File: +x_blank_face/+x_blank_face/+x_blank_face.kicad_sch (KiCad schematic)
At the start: 0 parts

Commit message: added schematic to +x and routed ish the schematic
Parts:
- added J1: Conn_01x08_Pin, CNN_GNSS_Footprint:DF13-8P, symbol Connector:Conn_01x08_Pin
- added J2, J3: Conn_01x02_Pin, CNN_GNSS_Footprint:TE_440055-2, symbol Connector:Conn_01x02_Pin
- added R1, R2, R3, R4: 75, CNN_GNSS_Footprint:UB3C-75RF1, symbol Device:R
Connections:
- new net +X Drain: J1.3 (Pin_3), J1.4 (Pin_4), R1.2, R2.2, R3.2, R4.2
- new net -X Serial Out: J1.5 (Pin_5), J1.6 (Pin_6), J2.2 (Pin_2), J3.2 (Pin_2)
- new net 12VPDM: J1.1 (Pin_1), J1.2 (Pin_2), R1.1, R2.1, R3.1, R4.1
- new net GND: J1.7 (Pin_7), J1.8 (Pin_8), J2.1 (Pin_1), J3.1 (Pin_1)

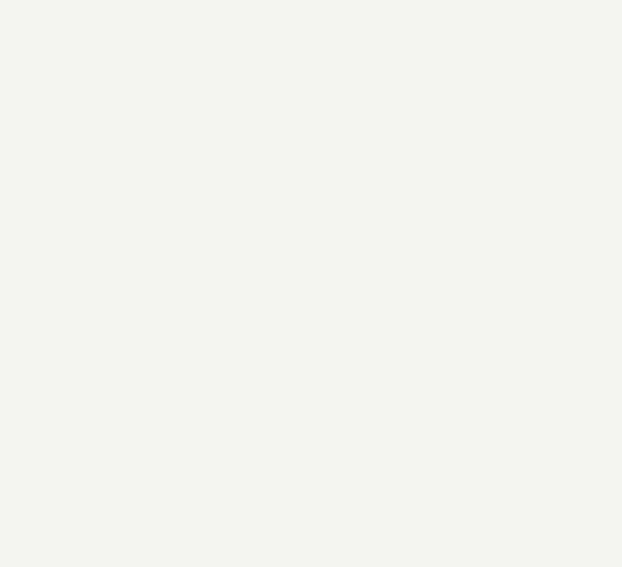
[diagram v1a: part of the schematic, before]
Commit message: Moved some things around, locked some components
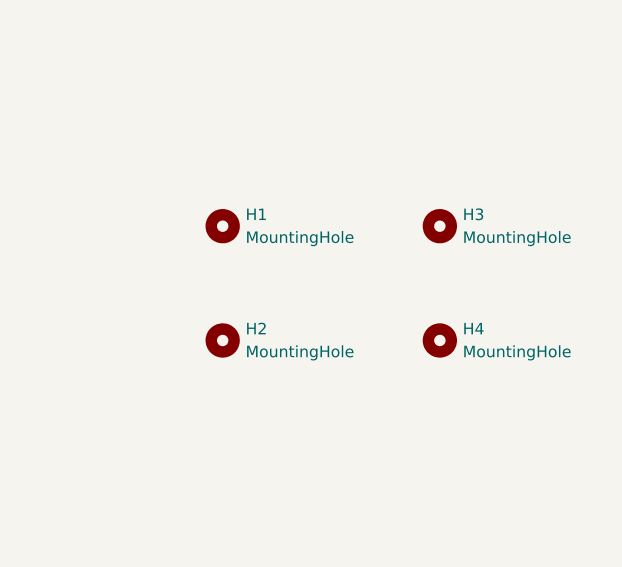
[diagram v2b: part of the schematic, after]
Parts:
- added H1, H2, H3, H4: MountingHole, CNN_GNSS_Footprint:2.55mm_Mounting_Hole, symbol Mechanical:MountingHole

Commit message: I forgot what I changed
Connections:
- net +X Drain: now also J1.5 (Pin_5), J1.6 (Pin_6); no longer J1.3 (Pin_3), J1.4 (Pin_4)
- net -X Serial Out: now also J1.3 (Pin_3), J1.4 (Pin_4); no longer J1.5 (Pin_5), J1.6 (Pin_6)
- net 12VPDM: now also J1.7 (Pin_7), J1.8 (Pin_8); no longer J1.1 (Pin_1), J1.2 (Pin_2)
- net GND: now also J1.1 (Pin_1), J1.2 (Pin_2); no longer J1.7 (Pin_7), J1.8 (Pin_8)
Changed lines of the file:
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@@
-	(wire
-		(pts
-			(xy 87.63 88.9) (xy 78.74 88.9)
-		)
-		(stroke
-			(width 0)
-			(type default)
-		)
-	)
 	(wire
 		(pts
@@
 	(wire
 		(pts
-			(xy 83.82 104.14) (xy 78.74 104.14)
-		)
-		(stroke
-			(width 0)
-			(type default)
-		)
-	)
-	(wire
-		(pts
-			(xy 81.28 91.44) (xy 78.74 91.44)
-		)
-		(stroke
-			(width 0)
-			(type default)
-		)
-	)
-	(wire
-		(pts
 			(xy 80.01 146.05) (xy 80.01 139.7)
 		)
@@
 	(wire
 		(pts
+			(xy 78.74 106.68) (xy 82.55 106.68)
+		)
+		(stroke
+			(width 0)
+			(type default)
+		)
+	)
+	(wire
+		(pts
+			(xy 78.74 104.14) (xy 83.82 104.14)
+		)
+		(stroke
+			(width 0)
+			(type default)
+		)
+	)
+	(wire
+		(pts
 			(xy 99.06 60.96) (xy 102.87 60.96)
 		)
@@
 	(wire
 		(pts
+			(xy 78.74 88.9) (xy 99.06 88.9)
+		)
+		(stroke
+			(width 0)
+			(type default)
+		)
+	)
+	(wire
+		(pts
 			(xy 95.25 60.96) (xy 99.06 60.96)
 		)
@@
 		(pts
 			(xy 76.2 137.16) (xy 90.17 137.16)
+		)
+		(stroke
+			(width 0)
+			(type default)
+		)
+	)
+	(wire
+		(pts
+			(xy 78.74 91.44) (xy 95.25 91.44)
 		)
 		(stroke
@@
 		)
 	)
-	(label "-X Serial Out"
-		(at 78.74 99.06 0)
-		(effects
-			(font
-				(size 1.27 1.27)
-			)
-			(justify left bottom)
-		)
-	)
 	(label "12VPDM"
-		(at 87.63 88.9 0)
+		(at 82.55 106.68 0)
 		(effects
 			(font
@@
 		)
 	)
-	(label "-X Serial Out"
+	(label "+X Drain"
 		(at 78.74 101.6 0)
 		(effects
@@
 	)
 	(label "-X Serial Out"
+		(at 78.74 93.98 0)
+		(effects
+			(font
+				(size 1.27 1.27)
+			)
+			(justify left bottom)
+		)
+	)
+	(label "-X Serial Out"
 		(at 80.01 146.05 0)
 		(effects
@@
 	)
 	(label "+X Drain"
-		(at 78.74 93.98 0)
+		(at 81.28 71.12 270)
+		(effects
+			(font
+				(size 1.27 1.27)
+			)
+			(justify right bottom)
+		)
+	)
+	(label "12VPDM"
+		(at 83.82 104.14 0)
+		(effects
+			(font
+				(size 1.27 1.27)
+			)
+			(justify left bottom)
+		)
+	)
+	(label "-X Serial Out"
+		(at 78.74 96.52 0)
 		(effects
 			(font
@@
 	)
 	(label "+X Drain"
-		(at 81.28 71.12 270)
-		(effects
-			(font
-				(size 1.27 1.27)
-			)
-			(justify right bottom)
-		)
-	)
-	(label "12VPDM"
-		(at 81.28 91.44 0)
-		(effects
-			(font
-				(size 1.27 1.27)
-			)
-			(justify left bottom)
-		)
-	)
-	(label "+X Drain"
-		(at 78.74 96.52 0)
+		(at 78.74 99.06 0)
 		(effects
 			(font
@@
 	(symbol
 		(lib_id "power:GND")
-		(at 78.74 106.68 0)
+		(at 95.25 91.44 0)
 		(unit 1)
 		(exclude_from_sim no)
@@
 		(dnp no)
 		(property "Reference" "#PWR04"
-			(at 78.74 113.03 0)
+			(at 95.25 97.79 0)
 			(effects
 				(font
@@
 		)
 		(property "Value" "GND"
-			(at 79.756 110.236 0)
+			(at 96.266 94.996 0)
 			(effects
 				(font
@@
 		)
 		(property "Footprint" ""
-			(at 78.74 106.68 0)
+			(at 95.25 91.44 0)
 			(effects
 				(font
@@
 		)
 		(property "Datasheet" ""
-			(at 78.74 106.68 0)
+			(at 95.25 91.44 0)
 			(effects
 				(font
@@
 		)
 		(property "Description" "Power symbol creates a global label with name \"GND\" , ground"
-			(at 78.74 106.68 0)
+			(at 95.25 91.44 0)
 			(effects
 				(font
@@
 	(symbol
 		(lib_id "power:GND")
-		(at 83.82 104.14 0)
+		(at 99.06 88.9 0)
 		(unit 1)
 		(exclude_from_sim no)
@@
 		(dnp no)
 		(property "Reference" "#PWR03"
-			(at 83.82 110.49 0)
+			(at 99.06 95.25 0)
 			(effects
 				(font
@@
 		)
 		(property "Value" "GND"
-			(at 85.598 107.442 0)
+			(at 100.838 92.202 0)
 			(effects
 				(font
@@
 		)
 		(property "Footprint" ""
-			(at 83.82 104.14 0)
+			(at 99.06 88.9 0)
 			(effects
 				(font
@@
 		)
 		(property "Datasheet" ""
-			(at 83.82 104.14 0)
+			(at 99.06 88.9 0)
 			(effects
 				(font
@@
 		)
 		(property "Description" "Power symbol creates a global label with name \"GND\" , ground"
-			(at 83.82 104.14 0)
-			(effects
-				(font
+			(at 99.06 88.9 0)
+			(effects
+				(font

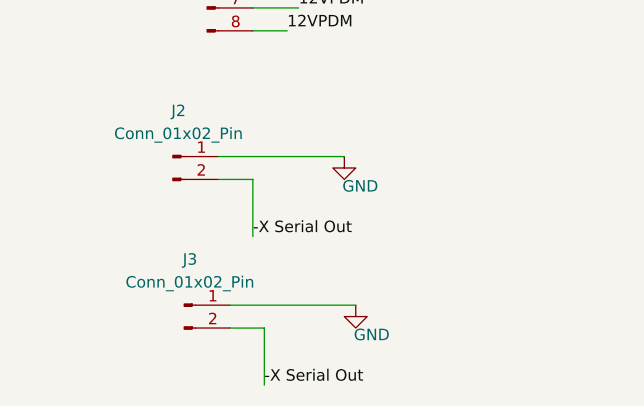
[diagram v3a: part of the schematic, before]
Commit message: Updated +X blank to remove GND and PWR plane, and changed parallel switches to series switches
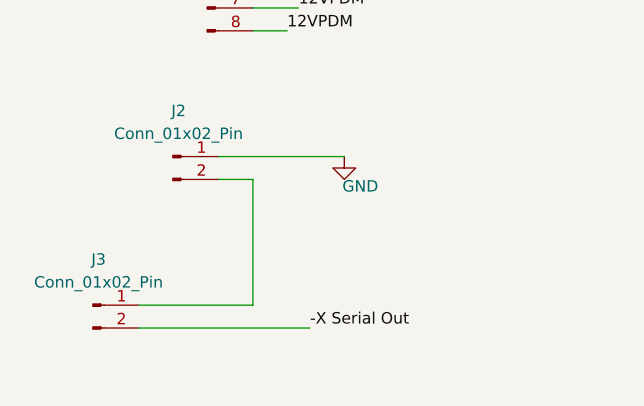
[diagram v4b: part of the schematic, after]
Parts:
- J2, J3: footprint CNN_GNSS_Footprint:TE_440055-2 -> CNN_GNSS_Footprint:CON2_1X2_UR_DF13
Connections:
- net -X Serial Out: no longer J2.2 (Pin_2)
- net GND: no longer J3.1 (Pin_1)
- new net: J2.2 (Pin_2), J3.1 (Pin_1)
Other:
- moved on the sheet: J3
